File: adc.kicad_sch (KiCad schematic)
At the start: 9 parts, among them U801 AD7357xRU

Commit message: Schematic update
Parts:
- C801, C802: footprint (none) -> Capacitor_SMD:CP_Elec_4x5.8; Spec2 LL-ELCO -> ELCO; Tolerance (none) -> 20%
- C803, C804: footprint Capacitor_SMD:C_0805_2012Metric -> Capacitor_SMD:C_1206_3216Metric; Spec1 10V -> 16V
- C805, C806, C807, C808: Spec1 (none) -> 16V; Spec2 (none) -> X5R; Tolerance (none) -> 20%
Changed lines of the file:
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@@
       (effects (font (size 1.27 1.27)) (justify left))
     )
-    (property "Footprint" "Capacitor_SMD:C_0805_2012Metric" (id 2) (at 134.3152 129.54 0)
+    (property "Footprint" "Capacitor_SMD:C_1206_3216Metric" (id 2) (at 134.3152 129.54 0)
       (effects (font (size 1.27 1.27)) hide)
     )
@@
       (effects (font (size 1.27 1.27)) hide)
     )
-    (property "Spec1" "10V" (id 5) (at 136.271 126.209 0)
+    (property "Spec1" "16V" (id 5) (at 136.271 126.209 0)
       (effects (font (size 1.27 1.27)) (justify left))
     )
@@
       (effects (font (size 1.27 1.27)) (justify right))
     )
-    (property "Footprint" "" (id 2) (at 121.6152 129.54 0)
+    (property "Footprint" "Capacitor_SMD:CP_Elec_4x5.8" (id 2) (at 121.6152 129.54 0)
       (effects (font (size 1.27 1.27)) hide)
     )
@@
       (effects (font (size 1.27 1.27)) (justify right))
     )
-    (property "Spec2" "LL-ELCO" (id 5) (at 117.729 129.4827 0)
-      (effects (font (size 1.27 1.27)) (justify right))
+    (property "Spec2" "ELCO" (id 5) (at 117.729 129.4827 0)
+      (effects (font (size 1.27 1.27)) (justify right))
+    )
+    (property "Tolerance" "20%" (id 6) (at 120.65 125.73 0)
+      (effects (font (size 1.27 1.27)) hide)
     )
     (pin "1")
@@
       (effects (font (size 1.27 1.27)) (justify left))
     )
-    (property "Footprint" "Capacitor_SMD:C_0805_2012Metric" (id 2) (at 134.3152 99.06 0)
+    (property "Footprint" "Capacitor_SMD:C_1206_3216Metric" (id 2) (at 134.3152 99.06 0)
       (effects (font (size 1.27 1.27)) hide)
     )
@@
       (effects (font (size 1.27 1.27)) hide)
     )
-    (property "Spec1" "10V" (id 5) (at 136.271 95.729 0)
+    (property "Spec1" "16V" (id 5) (at 136.271 95.729 0)
       (effects (font (size 1.27 1.27)) (justify left))
     )
@@
       (effects (font (size 1.27 1.27)) hide)
     )
+    (property "Spec1" "16V" (id 4) (at 149.86 44.45 0)
+      (effects (font (size 1.27 1.27)) hide)
+    )
+    (property "Spec2" "X5R" (id 5) (at 149.86 44.45 0)
+      (effects (font (size 1.27 1.27)) hide)
+    )
+    (property "Tolerance" "20%" (id 6) (at 149.86 44.45 0)
+      (effects (font (size 1.27 1.27)) hide)
+    )
     (pin "1")
     (pin "2")
@@
       (effects (font (size 1.27 1.27)) (justify right))
     )
-    (property "Footprint" "" (id 2) (at 121.6152 99.06 0)
+    (property "Footprint" "Capacitor_SMD:CP_Elec_4x5.8" (id 2) (at 121.6152 99.06 0)
       (effects (font (size 1.27 1.27)) hide)
     )
@@
       (effects (font (size 1.27 1.27)) (justify right))
     )
-    (property "Spec2" "LL-ELCO" (id 5) (at 117.729 99.0027 0)
-      (effects (font (size 1.27 1.27)) (justify right))
+    (property "Spec2" "ELCO" (id 5) (at 117.729 99.0027 0)
+      (effects (font (size 1.27 1.27)) (justify right))
+    )
+    (property "Tolerance" "20%" (id 6) (at 120.65 95.25 0)
+      (effects (font (size 1.27 1.27)) hide)
     )
     (pin "1")
@@
       (effects (font (size 1.27 1.27)) hide)
     )
+    (property "Spec1" "16V" (id 4) (at 180.34 44.45 0)
+      (effects (font (size 1.27 1.27)) hide)
+    )
+    (property "Spec2" "X5R" (id 5) (at 180.34 44.45 0)
+      (effects (font (size 1.27 1.27)) hide)
+    )
+    (property "Tolerance" "20%" (id 6) (at 180.34 44.45 0)
+      (effects (font (size 1.27 1.27)) hide)
+    )
     (pin "1")
     (pin "2")
@@
       (effects (font (size 1.27 1.27)) hide)
     )
+    (property "Spec1" "16V" (id 4) (at 167.64 44.45 0)
+      (effects (font (size 1.27 1.27)) hide)
+    )
+    (property "Spec2" "X5R" (id 5) (at 167.64 44.45 0)
+      (effects (font (size 1.27 1.27)) hide)
+    )
+    (property "Tolerance" "20%" (id 6) (at 167.64 44.45 0)
+      (effects (font (size 1.27 1.27)) hide)
+    )
     (pin "1")
     (pin "2")
@@
       (effects (font (size 1.27 1.27)) hide)
     )
+    (property "Spec1" "16V" (id 4) (at 137.16 44.45 0)
+      (effects (font (size 1.27 1.27)) hide)
+    )
+    (property "Spec2" "X5R" (id 5) (at 137.16 44.45 0)
+      (effects (font (size 1.27 1.27)) hide)
+    )
+    (property "Tolerance" "20%" (id 6) (at 137.16 44.45 0)
+      (effects (font (size 1.27 1.27)) hide)
+    )

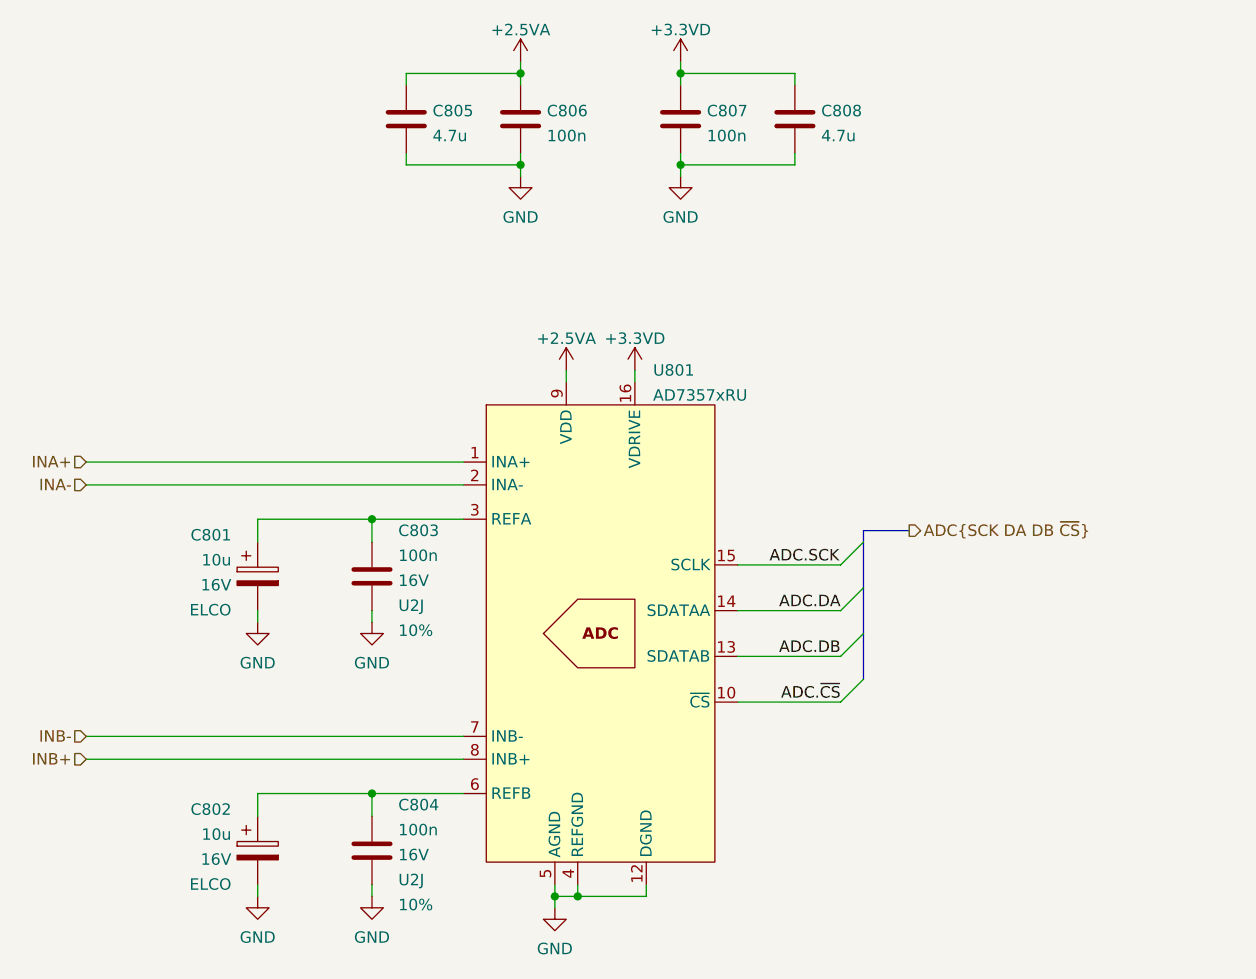
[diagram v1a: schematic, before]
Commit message: Schematic: better LDO output capacitor selection, clarified BOM
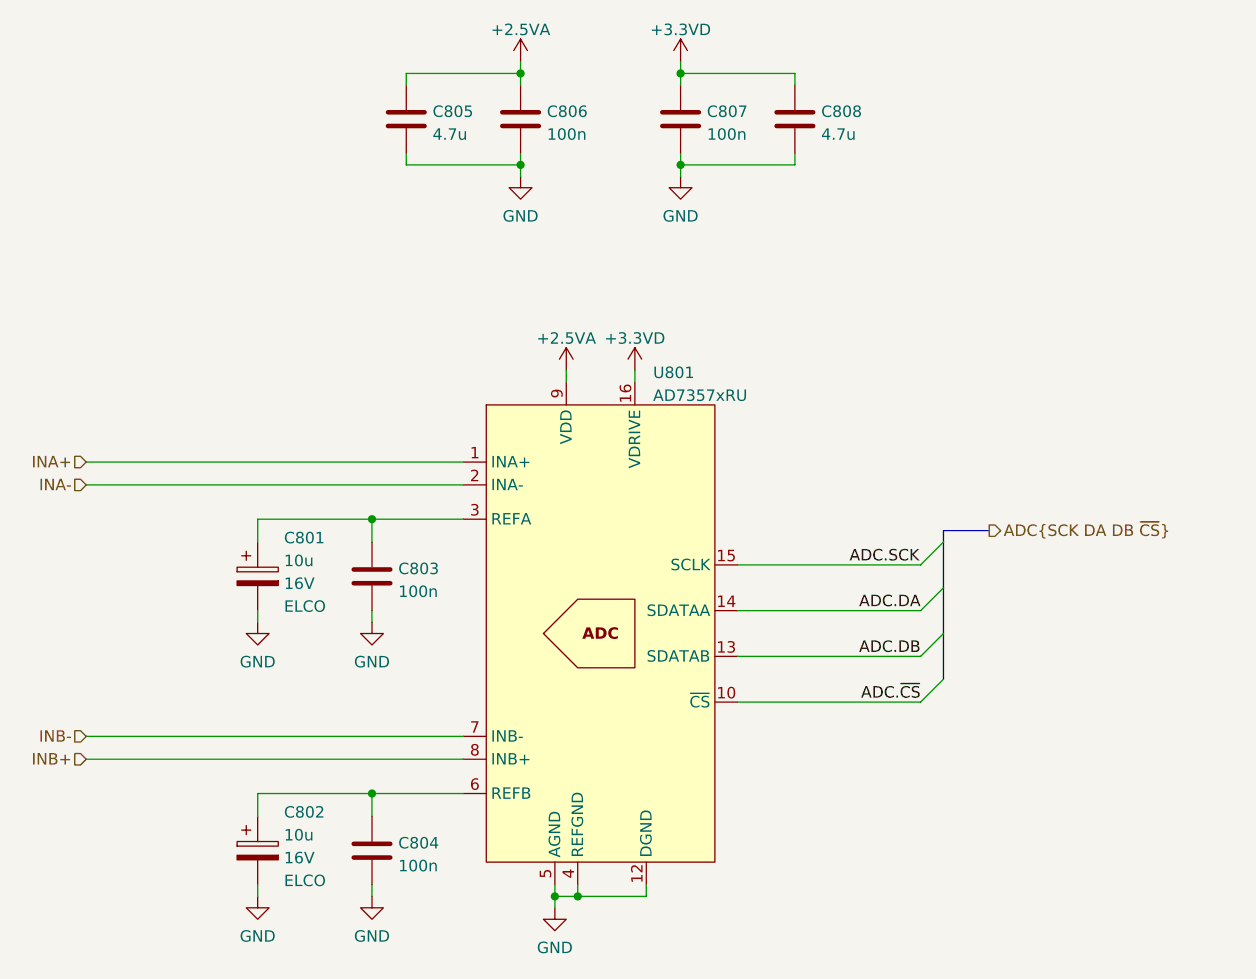
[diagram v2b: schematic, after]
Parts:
- C803, C804: footprint Capacitor_SMD:C_1206_3216Metric -> Capacitor_SMD:C_0805_2012Metric; Spec1 16V -> (none); Spec2 U2J -> (none); Tolerance 10% -> (none)
- C805, C806, C807, C808: Spec1 16V -> (none); Spec2 X5R -> (none); Tolerance 20% -> (none)

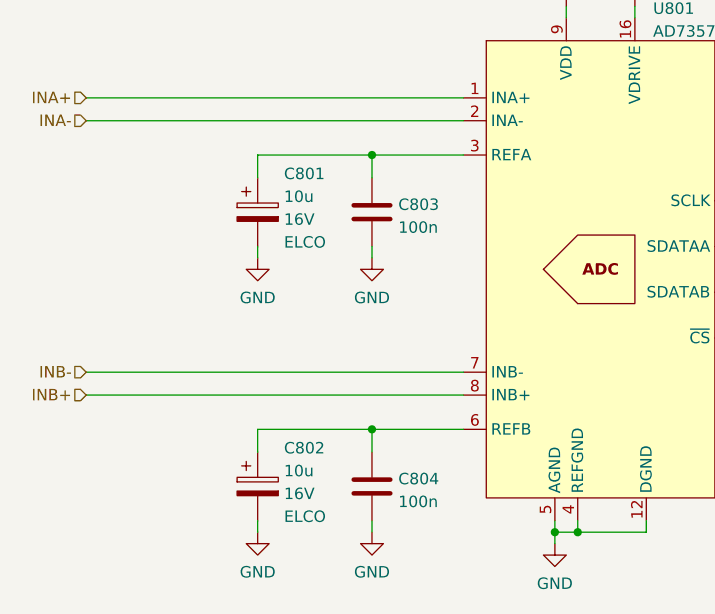
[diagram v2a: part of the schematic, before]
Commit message: Schematic: yet another update -Improve way caps are specified once again -Update cap voltages based on ESD simulation -Make anti-aliasing LC filter more practical - with much less inductors -Specify Mfr & MfrPN for almost all components (most from Mouser, some from Digikey)
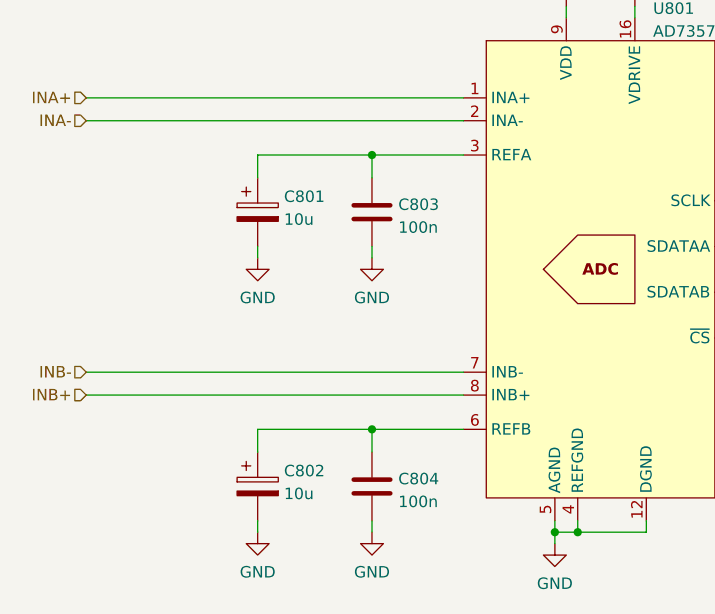
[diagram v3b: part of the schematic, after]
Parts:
- C801, C802: Mfr (none) -> Nichicon; Mfr PN (none) -> UCL1C100MCL1GS; Spec1 16V -> (none); Spec2 ELCO -> (none); Tolerance 20% -> (none)
- C803, C804, C806, C807: Mfr (none) -> Samsung; Mfr PN (none) -> CL21B104KBFNNNE
- C805, C808: Mfr (none) -> Murata; Mfr PN (none) -> GRM21BR71C475ME51
- U801: Mfr (none) -> Analog Devices; Mfr PN (none) -> AD7357BRUZ
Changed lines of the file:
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@@
   (symbol (lib_id "Device:C_Polarized") (at 120.65 125.73 0)
     (in_bom yes) (on_board yes) (fields_autoplaced)
-    (property "Reference" "C802" (id 0) (at 123.571 121.4694 0)
-      (effects (font (size 1.27 1.27)) (justify left))
-    )
-    (property "Value" "10u" (id 1) (at 123.571 124.0063 0)
+    (property "Reference" "C802" (id 0) (at 123.571 124.0063 0)
+      (effects (font (size 1.27 1.27)) (justify left))
+    )
+    (property "Value" "10u" (id 1) (at 123.571 126.5432 0)
       (effects (font (size 1.27 1.27)) (justify left))
     )
@@
       (effects (font (size 1.27 1.27)) hide)
     )
-    (property "Spec1" "16V" (id 4) (at 123.571 126.5432 0)
-      (effects (font (size 1.27 1.27)) (justify left))
-    )
-    (property "Spec2" "ELCO" (id 5) (at 123.571 129.0801 0)
-      (effects (font (size 1.27 1.27)) (justify left))
-    )
-    (property "Tolerance" "20%" (id 6) (at 120.65 125.73 0)
+    (property "Spec1" "" (id 4) (at 123.571 126.5432 0)
+      (effects (font (size 1.27 1.27)) (justify left))
+    )
+    (property "Spec2" "" (id 5) (at 123.571 129.0801 0)
+      (effects (font (size 1.27 1.27)) (justify left))
+    )
+    (property "Tolerance" "" (id 6) (at 120.65 125.73 0)
+      (effects (font (size 1.27 1.27)) hide)
+    )
+    (property "Mfr" "Nichicon" (id 7) (at 120.65 125.73 0)
+      (effects (font (size 1.27 1.27)) hide)
+    )
+    (property "Mfr PN" "UCL1C100MCL1GS" (id 8) (at 120.65 125.73 0)
       (effects (font (size 1.27 1.27)) hide)
     )
@@
       (effects (font (size 1.27 1.27)) hide)
     )
+    (property "Mfr" "Samsung" (id 8) (at 133.35 95.25 0)
+      (effects (font (size 1.27 1.27)) hide)
+    )
+    (property "Mfr PN" "CL21B104KBFNNNE" (id 9) (at 133.35 95.25 0)
+      (effects (font (size 1.27 1.27)) hide)
+    )
     (pin "1")
     (pin "2")
@@
     )
     (property "Datasheet" "https://www.analog.com/media/en/technical-documentation/data-sheets/AD7357.pdf" (id 3) (at 158.75 101.6 0)
+      (effects (font (size 1.27 1.27)) hide)
+    )
+    (property "Mfr" "Analog Devices" (id 4) (at 158.75 101.6 0)
+      (effects (font (size 1.27 1.27)) hide)
+    )
+    (property "Mfr PN" "AD7357BRUZ" (id 5) (at 158.75 101.6 0)
       (effects (font (size 1.27 1.27)) hide)
     )
@@
       (effects (font (size 1.27 1.27)) hide)
     )
+    (property "Mfr" "Samsung" (id 8) (at 133.35 125.73 0)
+      (effects (font (size 1.27 1.27)) hide)
+    )
+    (property "Mfr PN" "CL21B104KBFNNNE" (id 9) (at 133.35 125.73 0)
+      (effects (font (size 1.27 1.27)) hide)
+    )
     (pin "1")
     (pin "2")
@@
       (effects (font (size 1.27 1.27)) hide)
     )
+    (property "Mfr" "Samsung" (id 7) (at 149.86 44.45 0)
+      (effects (font (size 1.27 1.27)) hide)
+    )
+    (property "Mfr PN" "CL21B104KBFNNNE" (id 8) (at 149.86 44.45 0)
+      (effects (font (size 1.27 1.27)) hide)
+    )
     (pin "1")
     (pin "2")
@@
   (symbol (lib_id "Device:C_Polarized") (at 120.65 95.25 0)
     (in_bom yes) (on_board yes) (fields_autoplaced)
-    (property "Reference" "C801" (id 0) (at 123.571 90.9894 0)
-      (effects (font (size 1.27 1.27)) (justify left))
-    )
-    (property "Value" "10u" (id 1) (at 123.571 93.5263 0)
+    (property "Reference" "C801" (id 0) (at 123.571 93.5263 0)
+      (effects (font (size 1.27 1.27)) (justify left))
+    )
+    (property "Value" "10u" (id 1) (at 123.571 96.0632 0)
       (effects (font (size 1.27 1.27)) (justify left))
     )
@@
       (effects (font (size 1.27 1.27)) hide)
     )
-    (property "Spec1" "16V" (id 4) (at 123.571 96.0632 0)
-      (effects (font (size 1.27 1.27)) (justify left))
-    )
-    (property "Spec2" "ELCO" (id 5) (at 123.571 98.6001 0)
-      (effects (font (size 1.27 1.27)) (justify left))
-    )
-    (property "Tolerance" "20%" (id 6) (at 120.65 95.25 0)
+    (property "Spec1" "" (id 4) (at 123.571 96.0632 0)
+      (effects (font (size 1.27 1.27)) (justify left))
+    )
+    (property "Spec2" "" (id 5) (at 123.571 98.6001 0)
+      (effects (font (size 1.27 1.27)) (justify left))
+    )
+    (property "Tolerance" "" (id 6) (at 120.65 95.25 0)
+      (effects (font (size 1.27 1.27)) hide)
+    )
+    (property "Mfr" "Nichicon" (id 7) (at 120.65 95.25 0)
+      (effects (font (size 1.27 1.27)) hide)
+    )
+    (property "Mfr PN" "UCL1C100MCL1GS" (id 8) (at 120.65 95.25 0)
       (effects (font (size 1.27 1.27)) hide)
     )
@@
       (effects (font (size 1.27 1.27)) hide)
     )
+    (property "Mfr" "Murata" (id 7) (at 180.34 44.45 0)
+      (effects (font (size 1.27 1.27)) hide)
+    )
+    (property "Mfr PN" "GRM21BR71C475ME51" (id 8) (at 180.34 44.45 0)
+      (effects (font (size 1.27 1.27)) hide)
+    )
     (pin "1")
     (pin "2")
@@
       (effects (font (size 1.27 1.27)) hide)
     )
+    (property "Mfr" "Samsung" (id 7) (at 167.64 44.45 0)
+      (effects (font (size 1.27 1.27)) hide)
+    )
+    (property "Mfr PN" "CL21B104KBFNNNE" (id 8) (at 167.64 44.45 0)
+      (effects (font (size 1.27 1.27)) hide)
+    )
     (pin "1")
     (pin "2")
@@
       (effects (font (size 1.27 1.27)) hide)
     )
+    (property "Mfr" "Murata" (id 7) (at 137.16 44.45 0)
+      (effects (font (size 1.27 1.27)) hide)
+    )
+    (property "Mfr PN" "GRM21BR71C475ME51" (id 8) (at 137.16 44.45 0)
+      (effects (font (size 1.27 1.27)) hide)
+    )
